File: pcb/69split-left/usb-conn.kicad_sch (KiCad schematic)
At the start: 6 parts, among them J1 USB_C_Receptacle_USB2.0_14P

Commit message: Started layout?
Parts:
- added NT1: NetTie_2, NetTie:NetTie-2_SMD_Pad0.5mm, symbol Device:NetTie_2
- renumbered C1 to C8, J1 to J3, R3 to R10, R4 to R11, R1 to R8, R2 to R9
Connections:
- net VCC: now also NT1.1; no longer C8.1
- new net VBUS: C8.1, NT1.2
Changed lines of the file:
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@@
+	)
+	(junction
+		(at 92.71 118.11)
+		(diameter 0)
+		(color 0 0 0 0)
 	)
 	(junction
@@
 	)
 	(junction
-		(at 88.9 118.11)
+		(at 138.43 78.74)
 		(diameter 0)
 		(color 0 0 0 0)
@@
 	(wire
 		(pts
+			(xy 138.43 78.74) (xy 125.73 78.74)
+		)
+		(stroke
+			(width 0)
+			(type default)
+		)
+	)
+	(wire
+		(pts
 			(xy 116.84 96.52) (xy 116.84 97.79)
 		)
@@
 	(wire
 		(pts
+			(xy 153.67 78.74) (xy 138.43 78.74)
+		)
+		(stroke
+			(width 0)
+			(type default)
+		)
+	)
+	(wire
+		(pts
+			(xy 92.71 118.11) (xy 88.9 118.11)
+		)
+		(stroke
+			(width 0)
+			(type default)
+		)
+	)
+	(wire
+		(pts
+			(xy 92.71 118.11) (xy 96.52 118.11)
+		)
+		(stroke
+			(width 0)
+			(type default)
+		)
+	)
+	(wire
+		(pts
 			(xy 140.97 97.79) (xy 130.81 97.79)
 		)
@@
 	(wire
 		(pts
-			(xy 168.91 78.74) (xy 125.73 78.74)
-		)
-		(stroke
-			(width 0)
-			(type default)
-		)
-	)
-	(wire
-		(pts
-			(xy 88.9 118.11) (xy 96.52 118.11)
+			(xy 168.91 78.74) (xy 158.75 78.74)
 		)
 		(stroke
@@
 	(wire
 		(pts
-			(xy 88.9 119.38) (xy 88.9 118.11)
+			(xy 92.71 119.38) (xy 92.71 118.11)
 		)
 		(stroke
@@
 	(symbol
 		(lib_id "power:GND")
-		(at 88.9 119.38 0)
+		(at 92.71 119.38 0)
 		(mirror y)
 		(unit 1)
@@
 		(dnp no)
 		(fields_autoplaced yes)
-		(property "Reference" "#PWR01"
-			(at 88.9 125.73 0)
+		(property "Reference" "#PWR018"
+			(at 92.71 125.73 0)
 			(effects
 				(font
@@
 		)
 		(property "Value" "GND"
-			(at 91.44 120.6499 0)
+			(at 95.25 120.6499 0)
 			(effects
 				(font
@@
 		)
 		(property "Footprint" ""
-			(at 88.9 119.38 0)
+			(at 92.71 119.38 0)
 			(effects
 				(font
@@
 		)
 		(property "Datasheet" ""
-			(at 88.9 119.38 0)
+			(at 92.71 119.38 0)
 			(effects
 				(font
@@
 		)
 		(property "Description" ""
-			(at 88.9 119.38 0)
+			(at 92.71 119.38 0)
 			(effects
 				(font
@@
 			(project "69split-left"
 				(path "/94301c1c-44b1-4926-ac38-8a25b84a2b23/9761ff83-2474-42df-b43e-2f8540936a26"
-					(reference "#PWR01")
+					(reference "#PWR018")
 					(unit 1)
 				)
@@
 		(dnp no)
 		(fields_autoplaced yes)
-		(property "Reference" "R1"
+		(property "Reference" "R8"
 			(at 127 82.55 90)
 			(effects
@@
 			(project "69split-left"
 				(path "/94301c1c-44b1-4926-ac38-8a25b84a2b23/9761ff83-2474-42df-b43e-2f8540936a26"
-					(reference "R1")
+					(reference "R8")
 					(unit 1)
 				)
@@
 		(dnp no)
 		(fields_autoplaced yes)
-		(property "Reference" "R2"
+		(property "Reference" "R9"
 			(at 127 101.6 90)
 			(effects
@@
 			(project "69split-left"
 				(path "/94301c1c-44b1-4926-ac38-8a25b84a2b23/9761ff83-2474-42df-b43e-2f8540936a26"
-					(reference "R2")
+					(reference "R9")
 					(unit 1)
 				)
@@
 		(dnp no)
 		(fields_autoplaced yes)
-		(property "Reference" "#PWR02"
+		(property "Reference" "#PWR016"
 			(at 125.73 78.74 0)
 			(effects
@@
 			(project "69split-left"
 				(path "/94301c1c-44b1-4926-ac38-8a25b84a2b23/9761ff83-2474-42df-b43e-2f8540936a26"
-					(reference "#PWR02")
+					(reference "#PWR016")
 					(unit 1)
 				)
@@
 		(dnp no)
 		(fields_autoplaced yes)
-		(property "Reference" "J1"
+		(property "Reference" "J3"
 			(at 96.52 71.12 0)
 			(effects
@@
 			(project "69split-left"
 				(path "/94301c1c-44b1-4926-ac38-8a25b84a2b23/9761ff83-2474-42df-b43e-2f8540936a26"
-					(reference "J1")
+					(reference "J3")
 					(unit 1)
 				)
@@
 		(dnp no)
 		(fields_autoplaced yes)
-		(property "Reference" "#PWR04"
+		(property "Reference" "#PWR017"
 			(at 168.91 90.17 0)
 			(effects
@@
 			(project "69split-left"
 				(path "/94301c1c-44b1-4926-ac38-8a25b84a2b23/9761ff83-2474-42df-b43e-2f8540936a26"
-					(reference "#PWR04")
+					(reference "#PWR017")
 					(unit 1)
 				)
@@
 		(dnp no)
 		(fields_autoplaced yes)
-		(property "Reference" "R4"
+		(property "Reference" "R11"
 			(at 160.02 107.9499 0)
 			(effects
@@
 			(project "69split-left"
 				(path "/94301c1c-44b1-4926-ac38-8a25b84a2b23/9761ff83-2474-42df-b43e-2f8540936a26"
-					(reference "R4")
+					(reference "R11")
 					(unit 1)
 				)
@@
 		(dnp no)
 		(fields_autoplaced yes)
-		(property "Reference" "#PWR03"
+		(property "Reference" "#PWR019"
 			(at 154.94 138.43 0)
 			(effects
@@
 			(project "69split-left"
 				(path "/94301c1c-44b1-4926-ac38-8a25b84a2b23/9761ff83-2474-42df-b43e-2f8540936a26"
-					(reference "#PWR03")
+					(reference "#PWR019")
 					(unit 1)
 				)
@@
 		(dnp no)
 		(fields_autoplaced yes)
-		(property "Reference" "R3"
+		(property "Reference" "R10"
 			(at 149.86 102.8699 0)
 			(effects
@@
 			(project "69split-left"
 				(path "/94301c1c-44b1-4926-ac38-8a25b84a2b23/9761ff83-2474-42df-b43e-2f8540936a26"
-					(reference "R3")
+					(reference "R10")
+					(unit 1)
+				)
+			)
+		)
+	)
+	(symbol
+		(lib_id "power:PWR_FLAG")
+		(at 138.43 78.74 0)
+		(unit 1)
+		(exclude_from_sim no)
+		(in_bom yes)
+		(on_board yes)
+		(dnp no)
+		(fields_autoplaced yes)
+		(property "Reference" "#FLG01"
+			(at 138.43 76.835 0)
+			(effects
+				(font
+					(size 1.27 1.27)
+				)
+				(hide yes)
+			)
+		)
+		(property "Value" "PWR_FLAG"
+			(at 138.43 73.66 0)
+			(effects
+				(font
+					(size 1.27 1.27)
+				)
+			)
+		)
+		(property "Footprint" ""
+			(at 138.43 78.74 0)
+			(effects
+				(font
+					(size 1.27 1.27)
+				)
+				(hide yes)
+			)
+		)
+		(property "Datasheet" "~"
+			(at 138.43 78.74 0)
+			(effects
+				(font
+					(size 1.27 1.27)
+				)
+				(hide yes)
+			)
+		)
+		(property "Description" "Special symbol for telling ERC where power comes from"
+			(at 138.43 78.74 0)
+			(effects
+				(font
+					(size 1.27 1.27)
+				)
+				(hide yes)
+			)
+		)
+		(pin "1"
+		)
+		(instances
+			(project ""
+				(path "/94301c1c-44b1-4926-ac38-8a25b84a2b23/9761ff83-2474-42df-b43e-2f8540936a26"
+					(reference "#FLG01")
+					(unit 1)
+				)
+			)
+		)
+	)
+	(symbol
+		(lib_id "Device:NetTie_2")
+		(at 156.21 78.74 0)
+		(unit 1)
+		(exclude_from_sim no)
+		(in_bom no)
+		(on_board yes)
+		(dnp no)
+		(fields_autoplaced yes)
+		(property "Reference" "NT1"
+			(at 156.21 73.66 0)
+			(effects
+				(font
+					(size 1.27 1.27)
+				)
+			)
+		)
+		(property "Value" "NetTie_2"
+			(at 156.21 76.2 0)
+			(effects
+				(font
+					(size 1.27 1.27)
+				)
+			)
+		)
+		(property "Footprint" "NetTie:NetTie-2_SMD_Pad0.5mm"
+			(at 156.21 78.74 0)
+			(effects
+				(font
+					(size 1.27 1.27)
+				)
+				(hide yes)
+			)
+		)
+		(property "Datasheet" "~"
+			(at 156.21 78.74 0)
+			(effects
+				(font
+					(size 1.27 1.27)
+				)
+				(hide yes)
+			)
+		)
+		(property "Description" "Net tie, 2 pins"
+			(at 156.21 78.74 0)
+			(effects
+				(font
+					(size 1.27 1.27)
+				)
+				(hide yes)
+			)
+		)
+		(pin "2"
+		)
+		(pin "1"
+		)
+		(instances
+			(project ""
+				(path "/94301c1c-44b1-4926-ac38-8a25b84a2b23/9761ff83-2474-42df-b43e-2f8540936a26"
+					(reference "NT1")
 					(unit 1)
 				)
@@
 		(dnp no)
 		(fields_autoplaced yes)
-		(property "Reference" "C1"
+		(property "Reference" "C8"
 			(at 171.45 78.7462 0)
 			(effects
@@
 			(project "69split-left"
 				(path "/94301c1c-44b1-4926-ac38-8a25b84a2b23/9761ff83-2474-42df-b43e-2f8540936a26"
-					(reference "C1")
+					(reference "C8")
 					(unit 1)
 				)

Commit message: Continued layout.
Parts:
- removed NT1: NetTie_2, NetTie:NetTie-2_SMD_Pad0.5mm, symbol Device:NetTie_2
- C8: footprint Capacitor_SMD:C_0805_2012Metric_Pad1.18x1.45mm_HandSolder -> Capacitor_SMD:C_0603_1608Metric_Pad1.08x0.95mm_HandSolder
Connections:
- net VBUS is gone; now on net VCC: C8.1
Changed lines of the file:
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@@
 	)
 	(bus_alias "USB_BUS"
-		(members "VBUS" "D+" "D-")
+		(members "D+" "D-")
 	)
 	(text "USB CONNECTOR"
@@
 	)
 	(junction
+		(at 154.94 129.54)
+		(diameter 0)
+		(color 0 0 0 0)
+	)
+	(junction
+		(at 143.51 78.74)
+		(diameter 0)
+		(color 0 0 0 0)
+	)
+	(junction
 		(at 168.91 78.74)
 		(diameter 0)
@@
 	)
 	(junction
-		(at 154.94 129.54)
-		(diameter 0)
-		(color 0 0 0 0)
-	)
-	(junction
-		(at 138.43 78.74)
-		(diameter 0)
-		(color 0 0 0 0)
-	)
-	(junction
-		(at 125.73 78.74)
+		(at 88.9 118.11)
 		(diameter 0)
 		(color 0 0 0 0)
@@
 		)
 	)
-	(bus_entry
-		(at 226.06 93.98)
-		(size 2.54 2.54)
-		(stroke
-			(width 0)
-			(type default)
-		)
-	)
 	(wire
 		(pts
@@
 	(wire
 		(pts
-			(xy 125.73 74.93) (xy 125.73 78.74)
+			(xy 175.26 73.66) (xy 175.26 78.74)
 		)
 		(stroke
@@
 	(wire
 		(pts
-			(xy 210.82 93.98) (xy 226.06 93.98)
-		)
-		(stroke
-			(width 0)
-			(type default)
-		)
-	)
-	(wire
-		(pts
-			(xy 138.43 78.74) (xy 125.73 78.74)
-		)
-		(stroke
-			(width 0)
-			(type default)
-		)
-	)
-	(wire
-		(pts
 			(xy 116.84 96.52) (xy 116.84 97.79)
 		)
@@
 	(wire
 		(pts
-			(xy 179.07 78.74) (xy 168.91 78.74)
-		)
-		(stroke
-			(width 0)
-			(type default)
-		)
-	)
-	(wire
-		(pts
-			(xy 153.67 78.74) (xy 138.43 78.74)
-		)
-		(stroke
-			(width 0)
-			(type default)
-		)
-	)
-	(wire
-		(pts
 			(xy 92.71 118.11) (xy 88.9 118.11)
 		)
@@
 	(wire
 		(pts
-			(xy 111.76 78.74) (xy 125.73 78.74)
+			(xy 143.51 78.74) (xy 168.91 78.74)
+		)
+		(stroke
+			(width 0)
+			(type default)
+		)
+	)
+	(wire
+		(pts
+			(xy 111.76 78.74) (xy 143.51 78.74)
 		)
 		(stroke
@@
 	(wire
 		(pts
-			(xy 168.91 78.74) (xy 158.75 78.74)
-		)
-		(stroke
-			(width 0)
-			(type default)
-		)
-	)
-	(wire
-		(pts
 			(xy 111.76 93.98) (xy 116.84 93.98)
 		)
@@
 		)
 	)
+	(wire
+		(pts
+			(xy 154.94 132.08) (xy 154.94 129.54)
+		)
+		(stroke
+			(width 0)
+			(type default)
+		)
+	)
+	(wire
+		(pts
+			(xy 157.48 113.03) (xy 157.48 129.54)
+		)
+		(stroke
+			(width 0)
+			(type default)
+		)
+	)
+	(wire
+		(pts
+			(xy 116.84 92.71) (xy 123.19 92.71)
+		)
+		(stroke
+			(width 0)
+			(type default)
+		)
+	)
+	(wire
+		(pts
+			(xy 116.84 97.79) (xy 116.84 99.06)
+		)
+		(stroke
+			(width 0)
+			(type default)
+		)
+	)
+	(wire
+		(pts
+			(xy 152.4 129.54) (xy 154.94 129.54)
+		)
+		(stroke
+			(width 0)
+			(type default)
+		)
+	)
 	(bus
 		(pts
-			(xy 228.6 96.52) (xy 228.6 99.06)
-		)
-		(stroke
-			(width 0)
-			(type default)
-		)
-	)
-	(wire
-		(pts
-			(xy 154.94 132.08) (xy 154.94 129.54)
-		)
-		(stroke
-			(width 0)
-			(type default)
-		)
-	)
-	(wire
-		(pts
-			(xy 157.48 113.03) (xy 157.48 129.54)
-		)
-		(stroke
-			(width 0)
-			(type default)
-		)
-	)
-	(wire
-		(pts
-			(xy 116.84 92.71) (xy 123.19 92.71)
-		)
-		(stroke
-			(width 0)
-			(type default)
-		)
-	)
-	(wire
-		(pts
-			(xy 116.84 97.79) (xy 116.84 99.06)
-		)
-		(stroke
-			(width 0)
-			(type default)
-		)
-	)
-	(wire
-		(pts
-			(xy 152.4 129.54) (xy 154.94 129.54)
-		)
-		(stroke
-			(width 0)
-			(type default)
-		)
-	)
-	(bus
-		(pts
 			(xy 228.6 101.6) (xy 256.54 101.6)
 		)
@@
 		(pts
 			(xy 210.82 96.52) (xy 226.06 96.52)
+		)
+		(stroke
+			(width 0)
+			(type default)
+		)
+	)
+	(wire
+		(pts
+			(xy 168.91 78.74) (xy 175.26 78.74)
 		)
 		(stroke
@@
 	(label "D+"
 		(at 140.97 97.79 180)
-		(effects
-			(font
-				(size 1.27 1.27)
-			)
-			(justify right bottom)
-		)
-	)
-	(label "VBUS"
-		(at 210.82 93.98 0)
-		(effects
-			(font
-				(size 1.27 1.27)
-			)
-			(justify left bottom)
-		)
-	)
-	(label "VBUS"
-		(at 179.07 78.74 180)
 		(effects
 			(font
@@
 	(symbol
 		(lib_id "power:VCC")
-		(at 125.73 74.93 0)
+		(at 175.26 73.66 0)
 		(unit 1)
 		(exclude_from_sim no)
@@
 		(fields_autoplaced yes)
 		(property "Reference" "#PWR016"
-			(at 125.73 78.74 0)
+			(at 175.26 77.47 0)
 			(effects
 				(font
@@
 		)
 		(property "Value" "VCC"
-			(at 128.27 73.6599 0)
+			(at 177.8 72.3899 0)
 			(effects
 				(font
@@
 		)
 		(property "Footprint" ""
-			(at 125.73 74.93 0)
+			(at 175.26 73.66 0)
 			(effects
 				(font
@@
 		)
 		(property "Datasheet" ""
-			(at 125.73 74.93 0)
+			(at 175.26 73.66 0)
 			(effects
 				(font
@@
 		)
 		(property "Description" ""
-			(at 125.73 74.93 0)
+			(at 175.26 73.66 0)
 			(effects
 				(font
@@
 	(symbol
 		(lib_id "power:PWR_FLAG")
-		(at 138.43 78.74 0)
+		(at 143.51 78.74 0)
 		(unit 1)
 		(exclude_from_sim no)
@@
 		(fields_autoplaced yes)
 		(property "Reference" "#FLG01"
-			(at 138.43 76.835 0)
+			(at 143.51 76.835 0)
 			(effects
 				(font
@@
 		)
 		(property "Value" "PWR_FLAG"
-			(at 138.43 73.66 0)
+			(at 143.51 73.66 0)
 			(effects
 				(font
@@
 		)
 		(property "Footprint" ""
-			(at 138.43 78.74 0)
+			(at 143.51 78.74 0)
 			(effects
 				(font
@@
 		)
 		(property "Datasheet" "~"
-			(at 138.43 78.74 0)
+			(at 143.51 78.74 0)
 			(effects
 				(font
@@
 		)
 		(property "Description" "Special symbol for telling ERC where power comes from"
-			(at 138.43 78.74 0)
+			(at 143.51 78.74 0)
 			(effects
 				(font
@@
 	)
 	(symbol
-		(lib_id "Device:NetTie_2")
-		(at 156.21 78.74 0)
+		(lib_id "power:PWR_FLAG")
+		(at 88.9 118.11 90)
 		(unit 1)
 		(exclude_from_sim no)
-		(in_bom no)
+		(in_bom yes)
 		(on_board yes)
 		(dnp no)
 		(fields_autoplaced yes)
-		(property "Reference" "NT1"
-			(at 156.21 73.66 0)
-			(effects
-				(font
-					(size 1.27 1.27)
-				)
-			)
-		)
-		(property "Value" "NetTie_2"
-			(at 156.21 76.2 0)
-			(effects
-				(font
-					(size 1.27 1.27)
-				)
-			)
-		)
-		(property "Footprint" "NetTie:NetTie-2_SMD_Pad0.5mm"
-			(at 156.21 78.74 0)
+		(property "Reference" "#FLG03"
+			(at 86.995 118.11 0)
+			(effects
+				(font
+					(size 1.27 1.27)
+				)
+				(hide yes)
+			)
+		)
+		(property "Value" "PWR_FLAG"
+			(at 85.09 118.1099 90)
+			(effects
+				(font
+					(size 1.27 1.27)
+				)
+				(justify left)
+			)
+		)
+		(property "Footprint" ""
+			(at 88.9 118.11 0)
 			(effects
 				(font
@@
 		)
 		(property "Datasheet" "~"
-			(at 156.21 78.74 0)
-			(effects
-				(font
-					(size 1.27 1.27)
-				)
-				(hide yes)
-			)
-		)
-		(property "Description" "Net tie, 2 pins"
-			(at 156.21 78.74 0)
-			(effects
-				(font
-					(size 1.27 1.27)
-				)
-				(hide yes)
-			)
-		)
-		(pin "2"
+			(at 88.9 118.11 0)
+			(effects
+				(font
+					(size 1.27 1.27)
+				)
+				(hide yes)
+			)
+		)
+		(property "Description" "Special symbol for telling ERC where power comes from"
+			(at 88.9 118.11 0)
+			(effects
+				(font
+					(size 1.27 1.27)
+				)
+				(hide yes)
+			)
 		)
 		(pin "1"
 		)
 		(instances
-			(project ""
+			(project "69split-left"
 				(path "/94301c1c-44b1-4926-ac38-8a25b84a2b23/9761ff83-2474-42df-b43e-2f8540936a26"
-					(reference "NT1")
+					(reference "#FLG03")
 					(unit 1)
 				)
@@
 			)
 		)
-		(property "Footprint" "Capacitor_SMD:C_0805_2012Metric_Pad1.18x1.45mm_HandSolder"
+		(property "Footprint" "Capacitor_SMD:C_0603_1608Metric_Pad1.08x0.95mm_HandSolder"
 			(at 168.91 81.28 0)
 			(effects

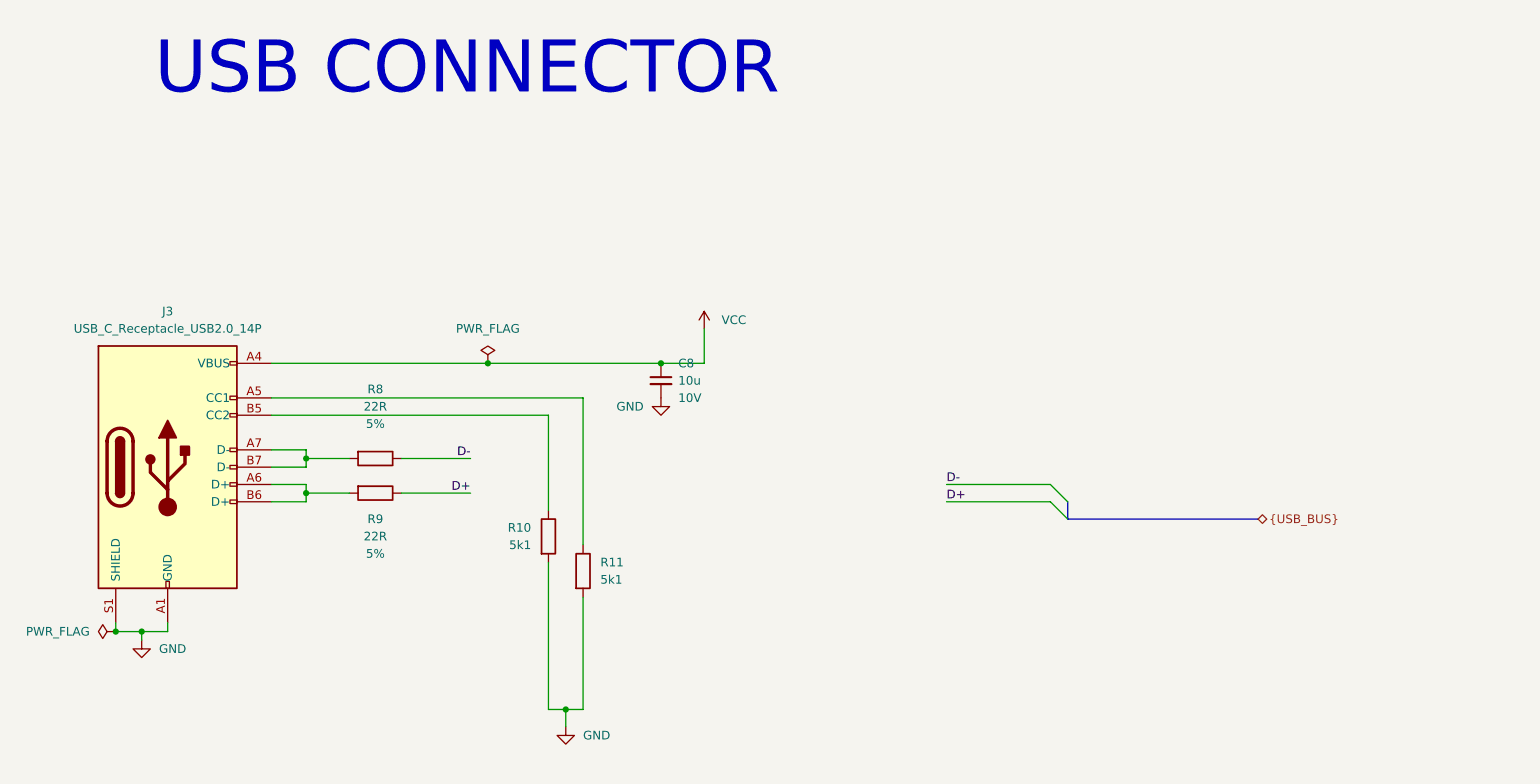
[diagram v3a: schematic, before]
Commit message: Practically finished the left side - need to make a footprint for the split USB connector. Some other schematic changes were made that I will not list. I should've made more commits between ths one and the previous one but it is what it is.
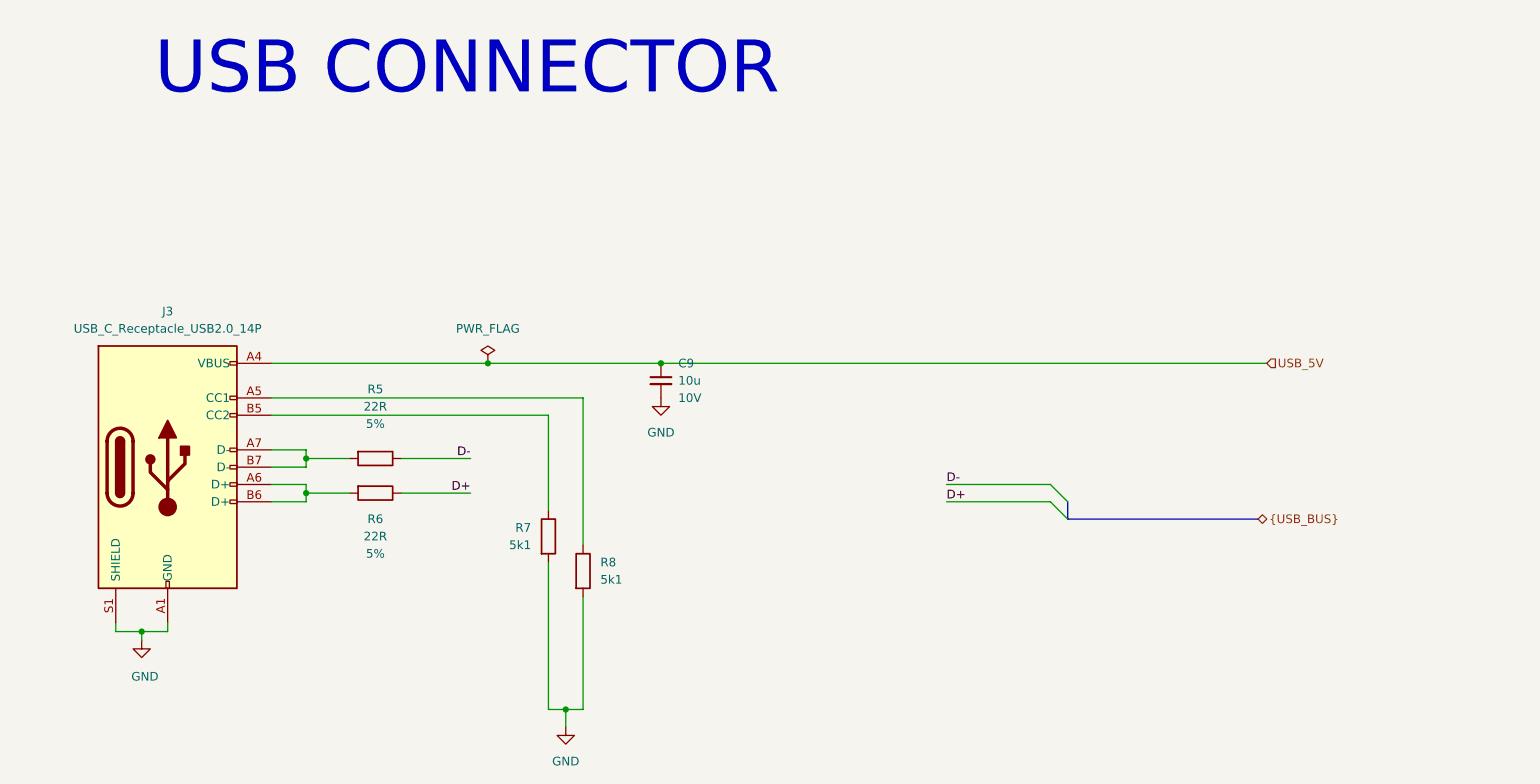
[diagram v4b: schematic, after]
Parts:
- renumbered C8 to C9, R8 to R5, R9 to R6, R10 to R7, R11 to R8
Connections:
- net VCC renamed USB_5V
